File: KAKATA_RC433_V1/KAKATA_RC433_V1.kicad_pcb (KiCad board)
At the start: 4 copper layers, 48 parts, among them U1 MKE04Z128VQH4, U10 74HC04, U2 MPU-6050_C24112, U3 433 MHz RF RECEIVER, U4 433 MHz TRANSMITTER, X1 X32258MOB4SI

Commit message: Actualizacion de componentes
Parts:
- removed H1: PROGRAMER, EasyEDA:HDR-TH_6P-P2.54-V-M
- removed H2: I2C_AUX, EasyEDA:HDR-TH_2P-P2.54-V-M
- removed H3: PWR, EasyEDA:HDR-TH_2P-P2.54-V-M
- removed ON/OFF1: MT-0-123-D001-D000-LF, EasyEDA:SW-TH_3P-L13.1-W8.0-P4.70_MT-0-102-F001-T000-RS
- removed U10: 74HC04, EasyEDA:SOIC-14_L8.7-W3.9-P1.27-LS6.0-BL
- added BT1: 2477, EasyEDA:BAT-TH_2477, B.Cu at (206.7, 180.0)
- added C13: C_0603, Capacitor_SMD_AKL:C_0603_1608Metric, F.Cu at (135.2, 213.6)
- added C14: C_0603, Capacitor_SMD_AKL:C_0603_1608Metric, F.Cu at (135.2, 216.3)
- added C15: C_0603, Capacitor_SMD_AKL:C_0603_1608Metric, F.Cu at (135.2, 219.1)
- added C16: C_0603, Capacitor_SMD_AKL:C_0603_1608Metric, F.Cu at (135.2, 221.8)
- added C17: C_0603, Capacitor_SMD_AKL:C_0603_1608Metric, F.Cu at (135.2, 224.5)
- added C18: C_0603, Capacitor_SMD_AKL:C_0603_1608Metric, F.Cu at (114.3, 221.4)
- added C19: C_0603, Capacitor_SMD_AKL:C_0603_1608Metric, F.Cu at (114.3, 224.1)
- added C20: C_0603, Capacitor_SMD_AKL:C_0603_1608Metric, F.Cu at (114.3, 226.8)
- added C21: C_0603, Capacitor_SMD_AKL:C_0603_1608Metric, F.Cu at (114.3, 229.5)
- added CN1: MG-JTAG-SWD6, MG_footprints:IDC-TH_6P-P2.54-V-R2-C3-S2.54, F.Cu at (138.2, 126.2)
- added R11: R_0603, Resistor_SMD_AKL:R_0603_1608Metric, F.Cu at (179.2, 126.5)
- added R16: R_0603, Resistor_SMD_AKL:R_0603_1608Metric, F.Cu at (110.1, 224.1)
- added R17: R_0603, Resistor_SMD_AKL:R_0603_1608Metric, F.Cu at (110.1, 226.8)
- added R18: R_0603, Resistor_SMD_AKL:R_0603_1608Metric, F.Cu at (110.1, 229.5)
- added SW1: ST-0-102-C03-N003-RS, EasyEDA:SW-TH_ST-0-102-C03-N003-RS, F.Cu at (200.0, 186.8)
- added SW2: EVQPUC02K, EasyEDA:SW-SMD_EVQPUD02K, F.Cu at (270.0, 116.2)
- added SW3: EVQPUC02K, EasyEDA:SW-SMD_EVQPUD02K, F.Cu at (279.8, 119.0)
- added SW4: EVQPUC02K, EasyEDA:SW-SMD_EVQPUD02K, F.Cu at (119.8, 119.5)
- added SW5: EVQPUC02K, EasyEDA:SW-SMD_EVQPUD02K, F.Cu at (129.2, 116.2)
- added U5: 74HC04, 4ms_Package_SOIC:SOIC-14_3.9x8.65mm_Pitch1.27mm, F.Cu at (173.5, 122.8)
- added U6: HS96L03W2C03, EasyEDA:OLED-TH_L27.8-W27.2-P2.54_C9900033791, F.Cu at (200.1, 150.5)
- added U7: LDL1117S33R, EasyEDA:SOT-223-4_L6.5-W3.5-P2.30-LS7.0-BR, F.Cu at (213.2, 186.8)
- C1, C2: value CL10C120JB8NNNC -> C_0603; footprint EasyEDA:C0603 -> Capacitor_SMD_AKL:C_0603_1608Metric
- C10, C11, C12, C3, C4, C5, C6, C7, C8, C9: footprint PCM_Capacitor_SMD_AKL:C_0603_1608Metric -> Capacitor_SMD_AKL:C_0603_1608Metric
- LED1, LED2, LED3, LED4, LED5, LED6: footprint EasyEDA:LED0603-FD -> LED_SMD:LED_0603_1608Metric
- R1, R10, R12, R13, R14, R15, R2, R3, R4, R5, R6, R7, R8, R9: footprint PCM_Resistor_SMD_AKL:R_0603_1608Metric -> Resistor_SMD_AKL:R_0603_1608Metric
- moved R15 171.2 mm to (110.1, 221.4)
- moved BTN2 160.3 mm to (227.1, 141.7)
- moved R6 152.7 mm to (89.5, 179.6)
- moved R7 152.7 mm to (89.5, 182.3)
- moved C6 150.7 mm to (168.3, 237.1)
- moved C7 150.7 mm to (157.8, 229.1)
- moved C10 150.7 mm to (182.2, 220.2)
- moved C11 150.7 mm to (182.5, 224.9)
- moved C12 150.7 mm to (174.5, 213.9)
- moved C3 150.7 mm to (182.5, 228.8)
- moved C4 150.7 mm to (182.5, 226.9)
- moved C5 150.7 mm to (182.5, 230.7)
- moved C8 150.7 mm to (176.3, 213.8)
- moved C9 150.7 mm to (182.2, 218.2)
- moved R10 150.7 mm to (221.8, 221.1)
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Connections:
- C1 pad 1: /EXTAL -> Net-(C1-Pad1)
- C2 pad 1: Net-(C2-Pad1) -> /EXTAL
- R1 pad 2: Net-(C2-Pad1) -> Net-(C1-Pad1)
- R12 pad 1: Net-(LED6-+) -> Net-(R12-Pad1)
- R12 pad 2: Net-(U10-3Y) -> Net-(LED5-+)
- R13 pad 1: Net-(LED5-+) -> Net-(R13-Pad1)
- R13 pad 2: Net-(U10-2Y) -> Net-(LED6-+)
- R14 pad 1: Net-(LED4-+) -> /BTN_3
- R14 pad 2: Net-(U10-1Y) -> +3.3V
- R15 pad 2: /BTN_1 -> /BTNL4
- R2 pad 1: Net-(C2-Pad1) -> /XTAL
- R2 pad 2: /XTAL -> Net-(C1-Pad1)
- R3 pad 1: Net-(LED1-+) -> Net-(R3-Pad1)
- R3 pad 2: Net-(U10-6Y) -> Net-(LED4-+)
- R5 pad 1: +3.3V -> /BTN_0
- R5 pad 2: /BTN_2 -> +3.3V
- R6 pad 1: +3.3V -> /BTN_1
- R6 pad 2: /BTN_0 -> +3.3V
- R7 pad 1: +3.3V -> /BTN_2
- R7 pad 2: /BTN_3 -> +3.3V
- R8 pad 1: Net-(LED2-+) -> Net-(R8-Pad1)
- R8 pad 2: Net-(U10-5Y) -> Net-(LED1-+)
- R9 pad 1: Net-(LED3-+) -> Net-(R9-Pad1)
- R9 pad 2: Net-(U10-4Y) -> Net-(LED2-+)
- U1 pad 40: unconnected-(U1-VSS-Pad40) -> GND
- U1 pad 41: unconnected-(U1-VDD-Pad41) -> +3.3V
- U1 pad 46: /LD1 -> /LED1
- U1 pad 7: unconnected-(U1-VDD-Pad7) -> +3.3V
- U1 pad 9: +3.3V -> GND
- U3 pad 5: unconnected-(U3-DO-Pad5) -> /RF_IN
- X1 pad 3: Net-(C2-Pad1) -> Net-(C1-Pad1)
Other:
- board outline added: 215.7 x 90.4 mm

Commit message: Teminado ruteo Terminado colocacion de REF Verifacadas las conexiones Verificados todos los errores conocidos Verificados los de clerance
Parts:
- removed CN1: MG-JTAG-SWD6, MG_footprints:IDC-TH_6P-P2.54-V-R2-C3-S2.54
- removed X1: X32258MOB4SI, EasyEDA:CRYSTAL-SMD_4P-L3.2-W2.5-BL
- added C22: 10uF, Capacitor_SMD_AKL:C_0805_2012Metric, F.Cu at (160.3, 118.9)
- added C23: 10nF, Capacitor_SMD_AKL:C_0603_1608Metric, F.Cu at (204.5, 164.8)
- added C24: 100nF, Capacitor_SMD_AKL:C_0603_1608Metric, F.Cu at (204.5, 162.8)
- added C25: 1uF, Capacitor_SMD_AKL:C_0603_1608Metric, F.Cu at (184.9, 117.6)
- added C26: 100nF, Capacitor_SMD_AKL:C_0603_1608Metric, F.Cu at (196.1, 186.9)
- added C27: 47uF, Capacitor_SMD_AKL:CP_Elec_6.3x5.2, F.Cu at (145.1, 137.7)
- added C28: 100nF, Capacitor_SMD_AKL:C_0603_1608Metric, F.Cu at (186.8, 127.0)
- added D1: ESD5B5.0S, Diode_SMD_AKL:D_SOD-523, F.Cu at (154.2, 119.4)
- added D2: B0540LW, Diode_SMD_AKL:D_SOD-123, F.Cu at (178.4, 188.0)
- added D3: ESD5B5.0S, Diode_SMD_AKL:D_SOD-523, F.Cu at (186.9, 129.9)
- added D4: ESD5B5.0S, Diode_SMD_AKL:D_SOD-523, F.Cu at (186.9, 132.8)
- added D5: B0540LW, Diode_SMD_AKL:D_SOD-123, F.Cu at (199.6, 185.2)
- added JP1: SolderJumper_2_Open, Jumper:SolderJumper-2_P1.3mm_Open_RoundedPad1.0x1.5mm, F.Cu at (184.4, 174.8)
- added JP2: SolderJumper_2_Open, Jumper:SolderJumper-2_P1.3mm_Open_RoundedPad1.0x1.5mm, F.Cu at (181.4, 174.8)
- added L1: HPC4018BM-3R3M, EasyEDA:IND-SMD_L4.0-W4.0_HPC4030NF, F.Cu at (184.2, 180.3)
- added R19: 5.1K, Resistor_SMD_AKL:R_0603_1608Metric, F.Cu at (173.5, 122.4)
- added R20: 5.1K, Resistor_SMD_AKL:R_0603_1608Metric, F.Cu at (164.1, 122.7)
- added R21: 33R, Resistor_SMD_AKL:R_0603_1608Metric, F.Cu at (184.0, 130.2)
- added R22: 33R, Resistor_SMD_AKL:R_0603_1608Metric, F.Cu at (184.0, 132.1)
- added R23: 10K, Resistor_SMD_AKL:R_0603_1608Metric, F.Cu at (184.9, 115.8)
- added R24: 100K, Resistor_SMD_AKL:R_0603_1608Metric, F.Cu at (179.6, 184.7)
- added R25: 22K, Resistor_SMD_AKL:R_0603_1608Metric, F.Cu at (188.5, 188.0)
- added R26: 100K, Resistor_SMD_AKL:R_0603_1608Metric, F.Cu at (217.7, 184.4)
- added R27: 22K, Resistor_SMD_AKL:R_0603_1608Metric, F.Cu at (217.7, 186.7)
- added U8: ESP32-S3-WROOM-1U-N16R2, EasyEDA:WIRELM-SMD_ESP32-S3-WROOM-1U, F.Cu at (200.1, 124.4)
- added USB1: TYPE-C 16PIN 2MD(073), EasyEDA:USB-C-SMD_TYPE-C-6PIN-2MD-073, F.Cu at (168.0, 117.9)
- C1, C10, C11, C12, C13, C16, C18, C19, C2, C20, C21, C3, C4, C5, C6, C7, C8, C9: value C_0603 -> 100nF
- C14, C15: value C_0603 -> 10uF; footprint Capacitor_SMD_AKL:C_0603_1608Metric -> Capacitor_SMD_AKL:C_0805_2012Metric
- C17: value C_0603 -> 47uF; footprint Capacitor_SMD_AKL:C_0603_1608Metric -> Capacitor_SMD_AKL:CP_Elec_6.3x5.2
- R1: value R_0603 -> 4.7k
- R11, R12, R13, R3, R8, R9: value R_0603 -> 220
- R14, R15, R16, R17, R18, R5, R6, R7: value R_0603 -> 22K
- R2: value R_0603 -> 4.7K
- U1: value MKE04Z128VQH4 -> MT3406; footprint EasyEDA:QFP-64_L14.0-W14.0-P0.80-LS17.2-BL -> EasyEDA:SOT-23-5_L2.9-W1.6-P0.95-LS2.8-BR
- moved R18 154.5 mm to (216.9, 117.9), turned to -90 degrees
- moved R17 154.0 mm to (218.9, 117.9), turned to -90 degrees
- moved R16 153.6 mm to (221.0, 117.9), turned to -90 degrees
- moved R15 153.2 mm to (223.0, 117.9), turned to -90 degrees
- moved C17 151.8 mm to (255.0, 131.3)
- moved C21 146.8 mm to (212.5, 120.4)
- moved C20 143.5 mm to (212.5, 122.2)
- moved R7 142.1 mm to (223.5, 135.2), turned to 90 degrees
- moved C19 140.2 mm to (212.5, 124.0)
- moved C18 137.1 mm to (212.5, 125.7)
- moved R6 136.6 mm to (225.6, 166.9), turned to 90 degrees
- moved C7 124.9 mm to (212.5, 116.9), turned to 0 degrees
- moved U4 112.7 mm to (130.5, 133.7), turned to 0 degrees
- moved C16 109.1 mm to (215.6, 148.1)
- moved C6 103.0 mm to (192.5, 136.9)
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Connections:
- C1 pad 1: Net-(C1-Pad1) -> +3.3V
- C10 pad 1: /ADC_JOY1_MD -> /ADC_JOY0_MD
- C11 pad 1: /BTN_1 -> /BTN_3
- C12 pad 1: /ADC_JOY0_MD -> /ADC_JOY0_MT
- C13 pad 1: +3.3V -> Net-(JP1-A)
- C14 pad 1: +3.3V -> Net-(JP2-A)
- C15 pad 1: +3.3V -> /vin
- C17 pad 1: Net-(U7-VIN) -> +3.3V
- C2 pad 1: /EXTAL -> Net-(U2-CPOUT)
- C3 pad 1: /BTN_2 -> /BTN_0
- C4 pad 1: /BTN_0 -> /BTN_1
- C5 pad 1: /BTN_3 -> /BTN_2
- C7 pad 1: /JOY1_BTN -> /ADC_JOY1_MD
- C8 pad 1: /ADC_JOY0_MT -> /ADC_JOY1_MT
- C9 pad 1: /ADC_JOY1_MT -> /JOY1_BTN
- R1 pad 1: /EXTAL -> +3.3V
- R1 pad 2: Net-(C1-Pad1) -> /I2C_SCL
- R2 pad 1: /XTAL -> +3.3V
- R2 pad 2: Net-(C1-Pad1) -> /I2C_SDA
- SW1 pad 2: Net-(BT1-+) -> Net-(D5-A)
- SW1 pad 3: Net-(U7-VIN) -> Net-(BT1-+)
- U1 pad 1: unconnected-(U1-PTD1-Pad1) -> /vin
- U1 pad 2: unconnected-(U1-PTD0-Pad2) -> GND
- U1 pad 3: unconnected-(U1-PTH7-Pad3) -> Net-(U1-SW)
- U1 pad 4: unconnected-(U1-PTH6-Pad4) -> /vin
- U1 pad 5: unconnected-(U1-PTE7-Pad5) -> Net-(U1-FB)
- U2 pad 1: unconnected-(U2-CLKIN-Pad1) -> GND
- U2 pad 10: unconnected-(U2-REGOUT-Pad10) -> Net-(U2-REGOUT)
- U2 pad 11: unconnected-(U2-FSYNC-Pad11) -> GND
- U2 pad 12: unconnected-(U2-INT-Pad12) -> /INT_MPU
- U2 pad 20: unconnected-(U2-CPOUT-Pad20) -> Net-(U2-CPOUT)
- U2 pad 23: /GYRO_SCL -> /I2C_SCL
- U2 pad 24: /GYRO_SDA -> /I2C_SDA
- U2 pad 25: unconnected-(U2-EP-Pad25) -> GND
- U2 pad 9: unconnected-(U2-AD0-Pad9) -> GND
- U3 pad 1: /ANT -> unconnected-(U3-ANT-Pad1)
- U3 pad 4: /RF_IN -> /DATA_RF_RECEIVED
- U3 pad 5: /RF_IN -> /DATA_RF_RECEIVED
- U4 pad 1: /RF_OUT -> /DATA_RF_SEND
- U4 pad 2: /ENABLE -> /RF_ENABLE
- U6 pad 3: /I2C1_SCL -> /I2C_SCL
- U6 pad 4: /I2C1_SDA -> /I2C_SDA
- U7 pad 2: +3.3V -> Net-(JP1-A)
- U7 pad 3: Net-(U7-VIN) -> /vin
- U7 pad 4: +3.3V -> Net-(JP1-A)
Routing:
- net /JOY1_BTN: track 0.00 -> 153.6 mm, vias 0 -> 3
- net /VBAT: track 0.00 -> 127.5 mm, vias 0 -> 2
- net /ADC_JOY0_MD: track 0.00 -> 123.7 mm, vias 0 -> 2
- net /BTNL2: track 0.00 -> 117.7 mm, vias 0 -> 2
- net VBUS: track 0.00 -> 108.4 mm
- net /BTNL1: track 0.00 -> 108.1 mm, vias 0 -> 2
- net /ADC_JOY1_MD: track 0.00 -> 105.6 mm, vias 0 -> 2
- net GND: track 0.00 -> 95.7 mm, vias 0 -> 91
- net /ADC_JOY1_MT: track 0.00 -> 94.9 mm, vias 0 -> 2
- net /BTN_1: track 0.00 -> 93.9 mm, vias 0 -> 2
- net /JOY0_BTN: track 0.00 -> 92.0 mm, vias 0 -> 2
- net /INT_MPU: track 0.00 -> 77.8 mm, vias 0 -> 4
- net /DATA_RF_RECEIVED: track 0.00 -> 77.7 mm, vias 0 -> 2
- net /BTNL3: track 0.00 -> 76.4 mm, vias 0 -> 2
- net /BTN_3: track 0.00 -> 75.0 mm, vias 0 -> 2
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- added copper zone on F.Cu, net +3.3V
- added copper zone on In2.Cu, net +3.3V
- added copper zone on F.Cu, net GND
- added copper zone on In1.Cu, net GND
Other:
- board text added: "RF-CONTROL V1"

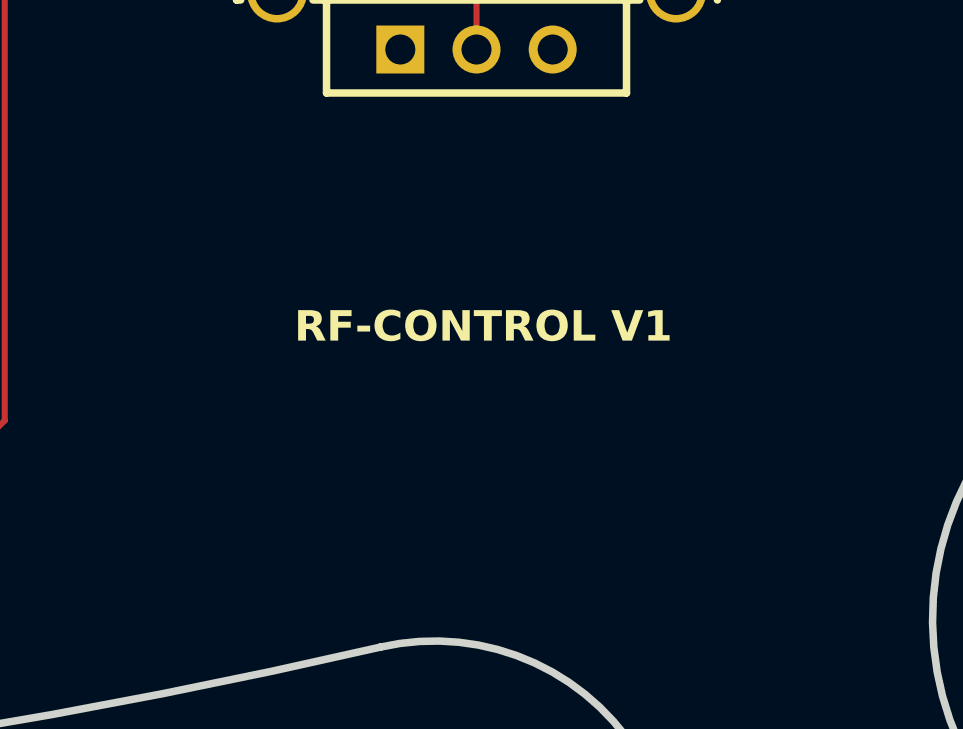
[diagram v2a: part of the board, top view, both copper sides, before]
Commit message: Agregada el texto de informacion en el layer SilkScreen Agregado la informacion en la hoja de diseno
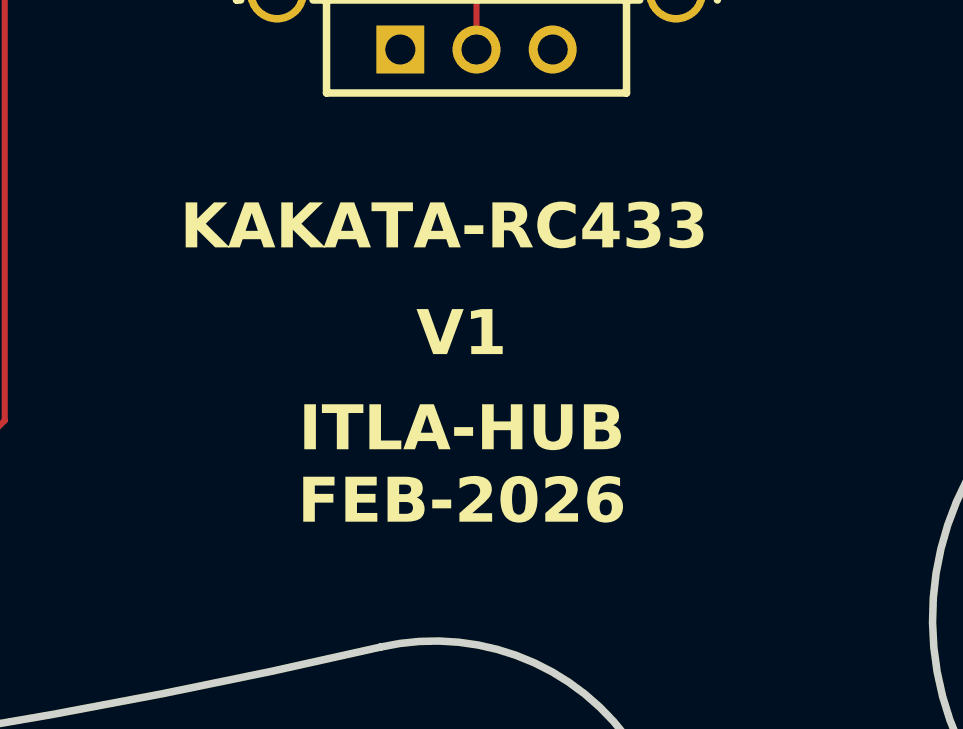
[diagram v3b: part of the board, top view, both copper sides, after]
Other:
- board text added: "ITLA-HUB FEB-2026"
- board text added: "KAKATA-RC433"
- board text added: "V1"
- board text removed: "RF-CONTROL V1"
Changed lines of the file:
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@@
 	)
 	(paper "USLedger")
+	(title_block
+		(title "KAKATA RC433")
+		(date "2026-02-22")
+		(rev "V1")
+		(company "ITLA-HUB")
+		(comment 1 "Desing: Carlos Pichardo")
+	)
 	(layers
 		(0 "F.Cu" signal)
@@
 		(at 193.802 180.594 -90)
 		(property "Reference" "U7"
-			(at -2.018 -3.108 180)
+			(at -2.018 -3.108 0)
 			(layer "F.SilkS")
 			(effects
@@
 		(model "${KICAD_3RD_PARTY}/EasyEDA.3dshapes/SOT-223-4P_L6.5-W3.5-H1.6-LS7.0-P2.30.wrl"
 			(offset
-				(xyz -941.76 660.4 -0)
+				(xyz 0 0 -0)
 			)
 			(scale
@@
 			)
 			(rotate
-				(xyz 0 0 180)
+				(xyz -0 -0 180)
 			)
 		)
@@
 		(model "${EASYEDA2KICAD}/easyeda2kicad.3dshapes/USB-C-SMD_TYPE-C-6PIN-2MD-073.wrl"
 			(offset
-				(xyz 0 -1.2 0.9)
+				(xyz -2.54 -3.104999988 -1.004999997)
 			)
 			(scale
@@
 			)
 			(rotate
-				(xyz 0 0 0)
+				(xyz -0 180 180)
+			)
+		)
+		(model "C:/DATA/RESOURCE/KiCAD/KICAD_3RD_PARTY/EasyEDA.3dshapes/USB-C-SMD_TYPE-C-6PIN-2MD-073.wrl"
+			(offset
+				(xyz 0 -1.27 1.778)
+			)
+			(scale
+				(xyz 1 1 1)
+			)
+			(rotate
+				(xyz -0 -0 -0)
 			)
 		)
@@
 		)
 		(embedded_fonts no)
-		(model "Housings_SOIC.3dshapes/SOIC-16_3.9x9.9mm_Pitch1.27mm.wrl"
+		(model "C:/Program Files/KiCad/9.0/share/kicad/3dmodels/Package_SO.3dshapes/SOIC-14_3.9x8.7mm_P1.27mm.wrl"
 			(offset
 				(xyz 0 0 0)
@@
 		(layer "User.1")
 	)
-	(gr_text "RF-CONTROL V1"
-		(at 248.726 175.528 0)
+	(gr_text "V1"
+		(at 252.79 176.036 0)
+		(layer "F.SilkS")
+		(effects
+			(font
+				(size 1.5 1.5)
+				(thickness 0.3)
+				(bold yes)
+			)
+			(justify left bottom)
+		)
+	)
+	(gr_text "KAKATA-RC433"
+		(at 244.916 172.48 0)
 		(layer "F.SilkS")
 		(effects
 			(font
-				(size 1.016 1.016)
-				(thickness 0.2032)
+				(size 1.5 1.5)
+				(thickness 0.3)
 				(bold yes)
 			)
@@
 		)
 	)
+	(gr_text "ITLA-HUB\nFEB-2026"
+		(at 254.314 181.624 0)
+		(layer "F.SilkS")
+		(effects
+			(font
+				(size 1.5 1.5)
+				(thickness 0.3)
+				(bold yes)
+			)
+			(justify bottom)
+		)
+	)

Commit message: Completado el BOM
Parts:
- moved C18 1.13 mm to (213.7, 125.7)
- moved SW1 0.44 mm to (206.0, 187.2)
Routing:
- net /I2C_SCL: track 59.9 -> 78.9 mm, vias 2 -> 4
- net /I2C_SDA: track 60.9 -> 78.4 mm, vias 2 -> 4
- net /JOY1_BTN: track 153.6 -> 149.9 mm
- net +3.3V: track 48.0 -> 44.7 mm
- net /INT_MPU: track 77.8 -> 79.9 mm
- net Net-(BT1-+): track 12.0 -> 13.5 mm
- net GND: track 95.7 -> 94.3 mm
- net Net-(D5-A): track 8.57 -> 7.57 mm
- net /vin: track 43.3 -> 44.0 mm
